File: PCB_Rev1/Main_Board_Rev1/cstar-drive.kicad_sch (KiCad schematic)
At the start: 0 parts

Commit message: Motor Drive Circuit
L298N motor driver and motor connections added
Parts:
- added C1: C_Polarized, symbol Device:C_Polarized
- added CR1, CR2: SP4022-01FTG-C, CSTAR-MainBoard-Footprints:ZDO_SP4022_LTF, symbol SP4022_01FTG_C:SP4022-01FTG-C
- added D1, D2, D3, D4, D5, D6, D7, D8: D, symbol Device:D
- added U1: L298N, Package_TO_SOT_THT:TO-220-15_P2.54x2.54mm_StaggerOdd_Lead4.58mm_Vertical, symbol Driver_Motor:L298N
- added X1, X2: B2P-VH, CSTAR-MainBoard-Footprints:B2P-VH, symbol B2P-VH:B2P-VH
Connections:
- new net +5V: C1.1, D1.1 (K), D2.1 (K), D3.1 (K), D4.1 (K), U1.4 (Vs), U1.9 (Vss)
- new net EN_MOTOR_1: U1.6 (EnA)
- new net EN_MOTOR_2: U1.11 (EnB)
- new net GND: C1.2, D5.2 (A), D6.2 (A), D7.2 (A), D8.2 (A), U1.1 (SENSE_A), U1.15 (SENSE_B), U1.8 (GND)
- new net IN1_MOTOR_1: U1.5 (IN1)
- new net IN1_MOTOR_2: U1.10 (IN3)
- new net IN2_MOTOR_1: U1.7 (IN2)
- new net IN2_MOTOR_2: U1.12 (IN4)
- new net OUT1_MOTOR_1: CR1.2, D1.2 (A), D5.1 (K), U1.2 (OUT1), X1.1
- new net OUT1_MOTOR_2: CR2.2, D3.2 (A), D7.1 (K), U1.13 (OUT3), X2.1
- new net OUT2_MOTOR_1: CR1.1, D2.2 (A), D6.1 (K), U1.3 (OUT2), X1.2
- new net OUT2_MOTOR_2: CR2.1, D4.2 (A), D8.1 (K), U1.14 (OUT4), X2.2
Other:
- note added: "MOTOR 1 CONNECTION"
- note added: "MOTOR 2 CONNECTION"
- note added: "MOTOR DRIVE TRAIN SCHEMATIC"
- note added: "MOTOR DRIVER"

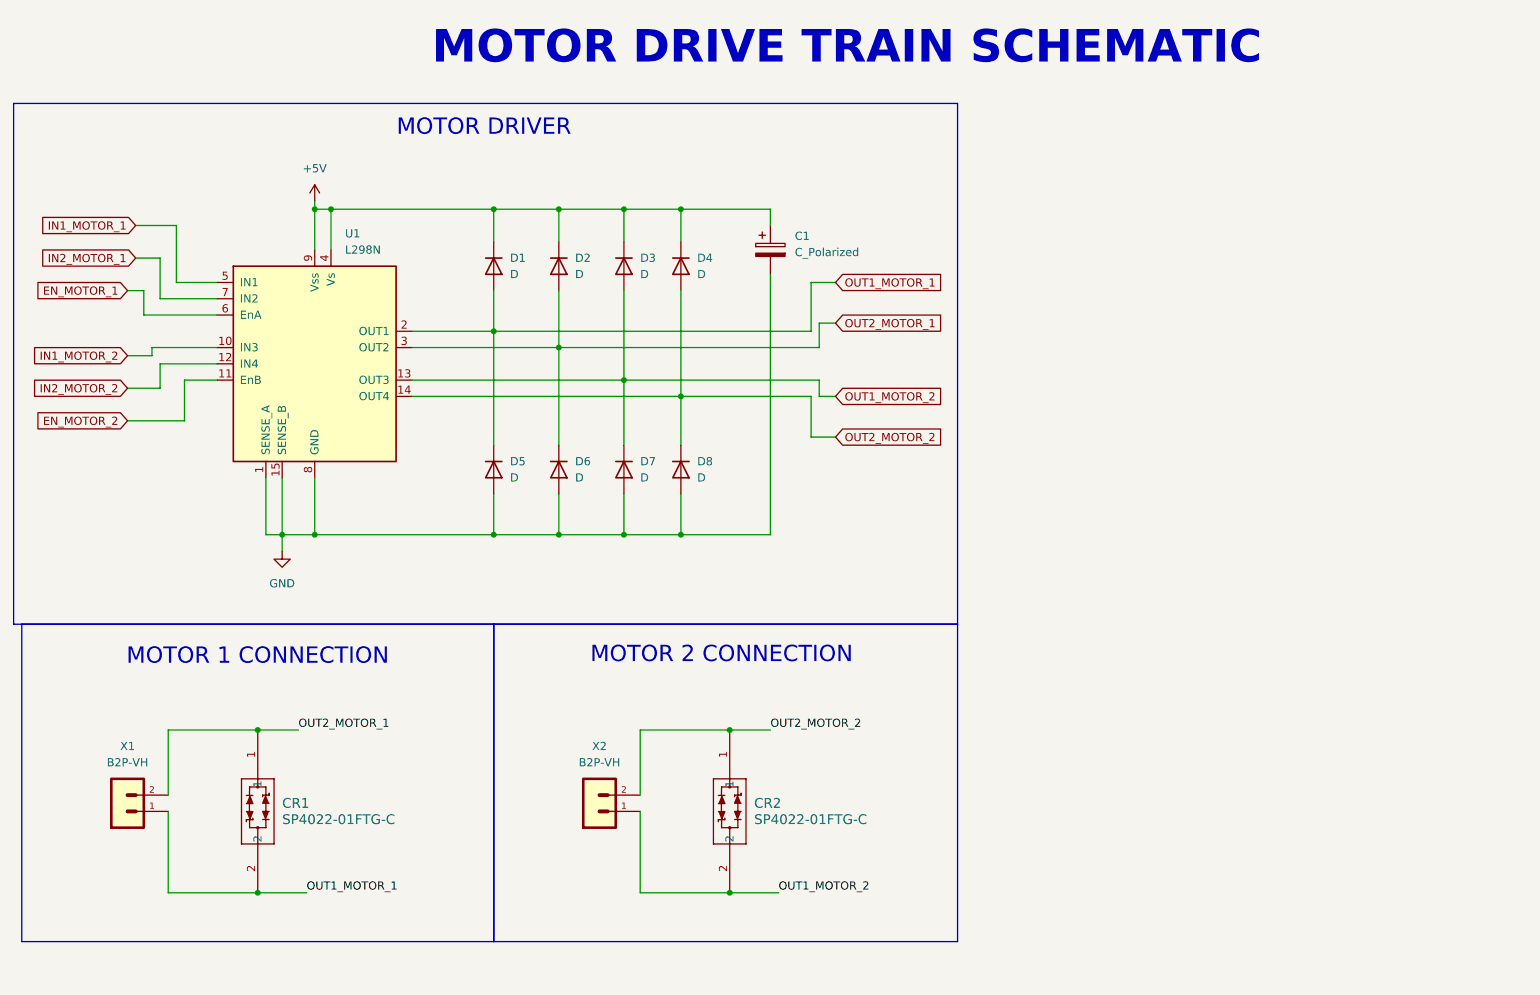
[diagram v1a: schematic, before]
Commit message: Motor Drive Update
Encoder connections added
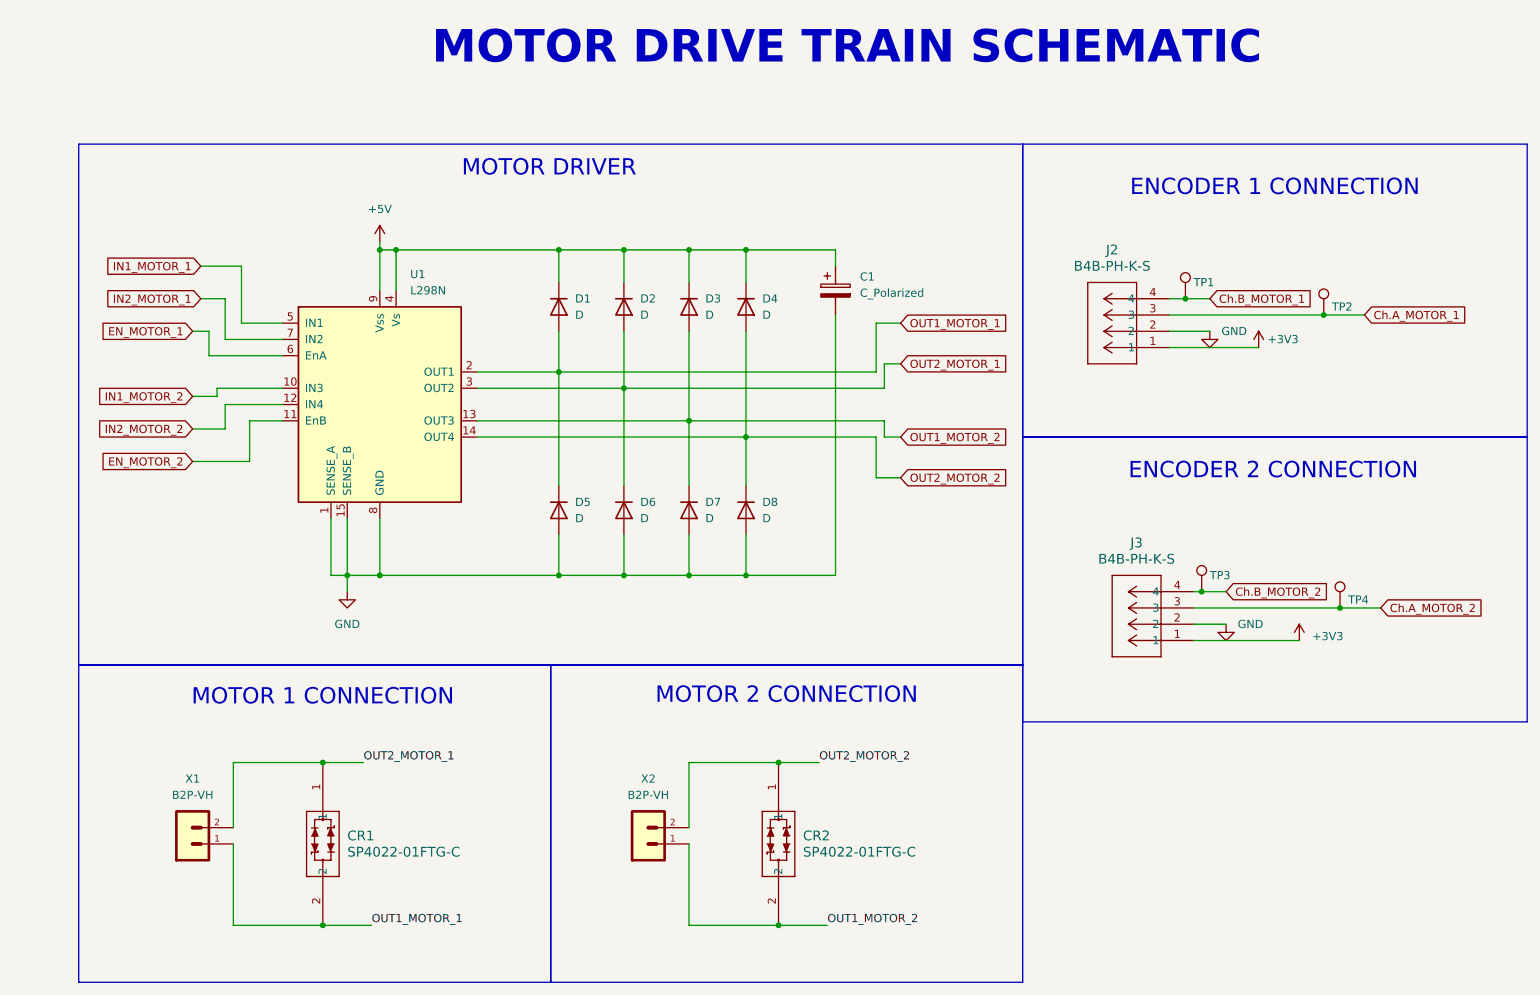
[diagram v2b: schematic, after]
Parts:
- added J2, J3: B4B-PH-K-S, CSTAR-MainBoard-Footprints:B4B_PH_K_S, symbol B4B_PH_K_S:B4B-PH-K-S
- added TP1: Ch.B MOTOR 1, TestPoint:TestPoint_Pad_D2.0mm, symbol Connector:TestPoint
- added TP2: Ch.A MOTOR 1, TestPoint:TestPoint_Pad_D2.0mm, symbol Connector:TestPoint
- added TP3: Ch.B MOTOR 2 TP, TestPoint:TestPoint_Pad_D2.0mm, symbol Connector:TestPoint
- added TP4: Ch.A MOTOR 2, TestPoint:TestPoint_Pad_D2.0mm, symbol Connector:TestPoint
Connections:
- net GND: now also J2.2, J3.2
- new net +3V3: J2.1, J3.1
- new net Ch.A_MOTOR_1: J2.3, TP2.1
- new net Ch.A_MOTOR_2: J3.3, TP4.1
- new net Ch.B_MOTOR_1: J2.4, TP1.1
- new net Ch.B_MOTOR_2: J3.4, TP3.1
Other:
- note added: "ENCODER 1 CONNECTION"
- note added: "ENCODER 2 CONNECTION"
- moved on the sheet: C1, CR1, CR2, D1, D2, D3, D4, D5, D6, D7, D8, U1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
